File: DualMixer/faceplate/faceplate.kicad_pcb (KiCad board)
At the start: 2 copper layers, 40.3 x 128.5 mm, 20 parts

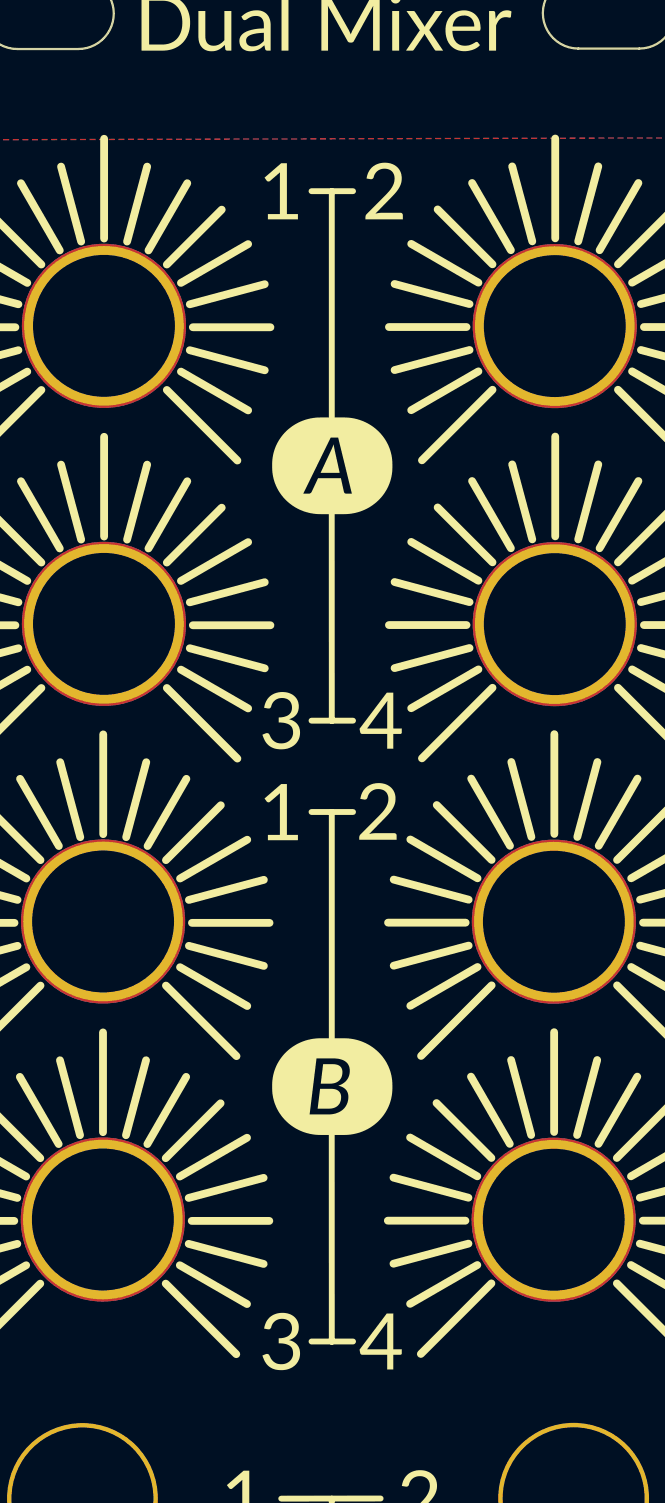
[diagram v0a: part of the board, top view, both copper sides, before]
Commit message: Add M3 mount for mechanical stability, and update power
This time for the DualMixer as well, it could do with extra supports
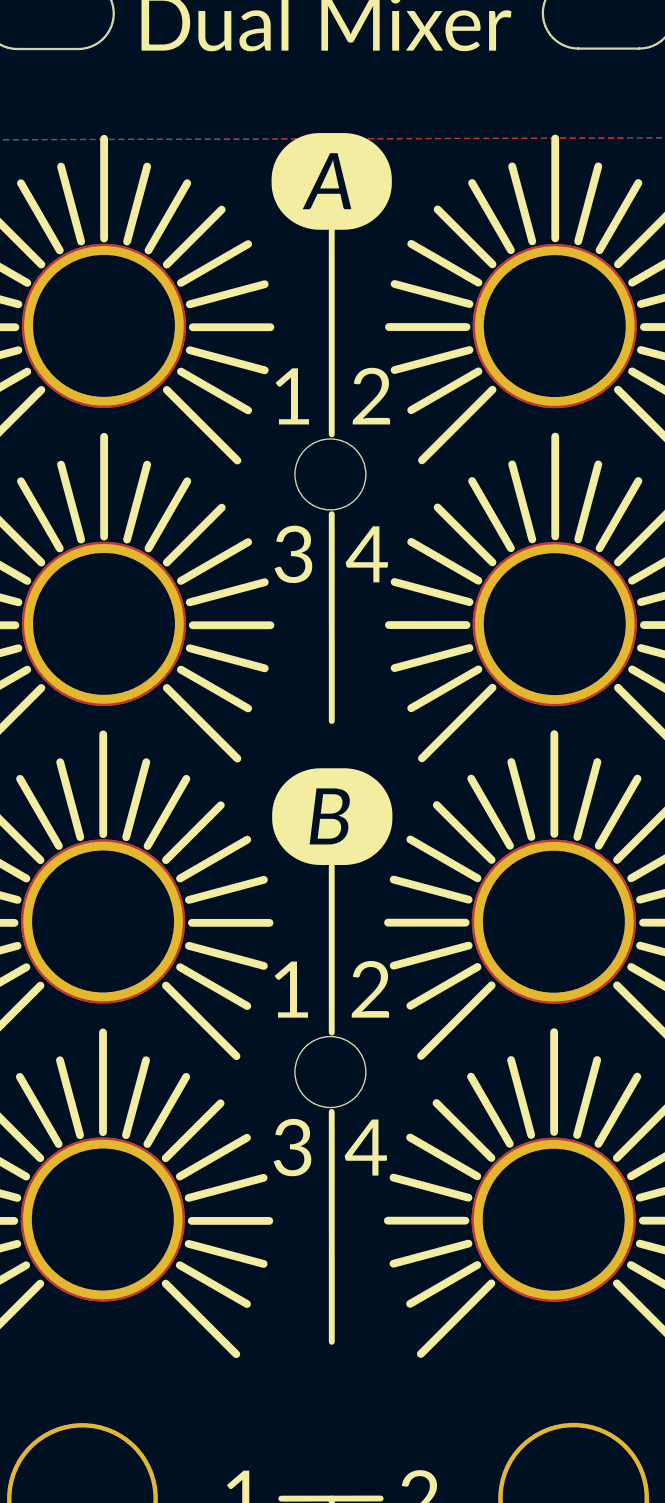
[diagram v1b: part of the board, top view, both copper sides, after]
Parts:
- added REF**: MountingHole_3.2mm_M3_NoCourt, Library:MountingHole_3.2mm_M3_NoCourt, F.Cu at (81.5, 90.8)
- added REF**: MountingHole_3.2mm_M3_NoCourt, Library:MountingHole_3.2mm_M3_NoCourt, F.Cu at (81.5, 63.8)
